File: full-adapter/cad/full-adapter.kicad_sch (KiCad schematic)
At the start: 0 parts

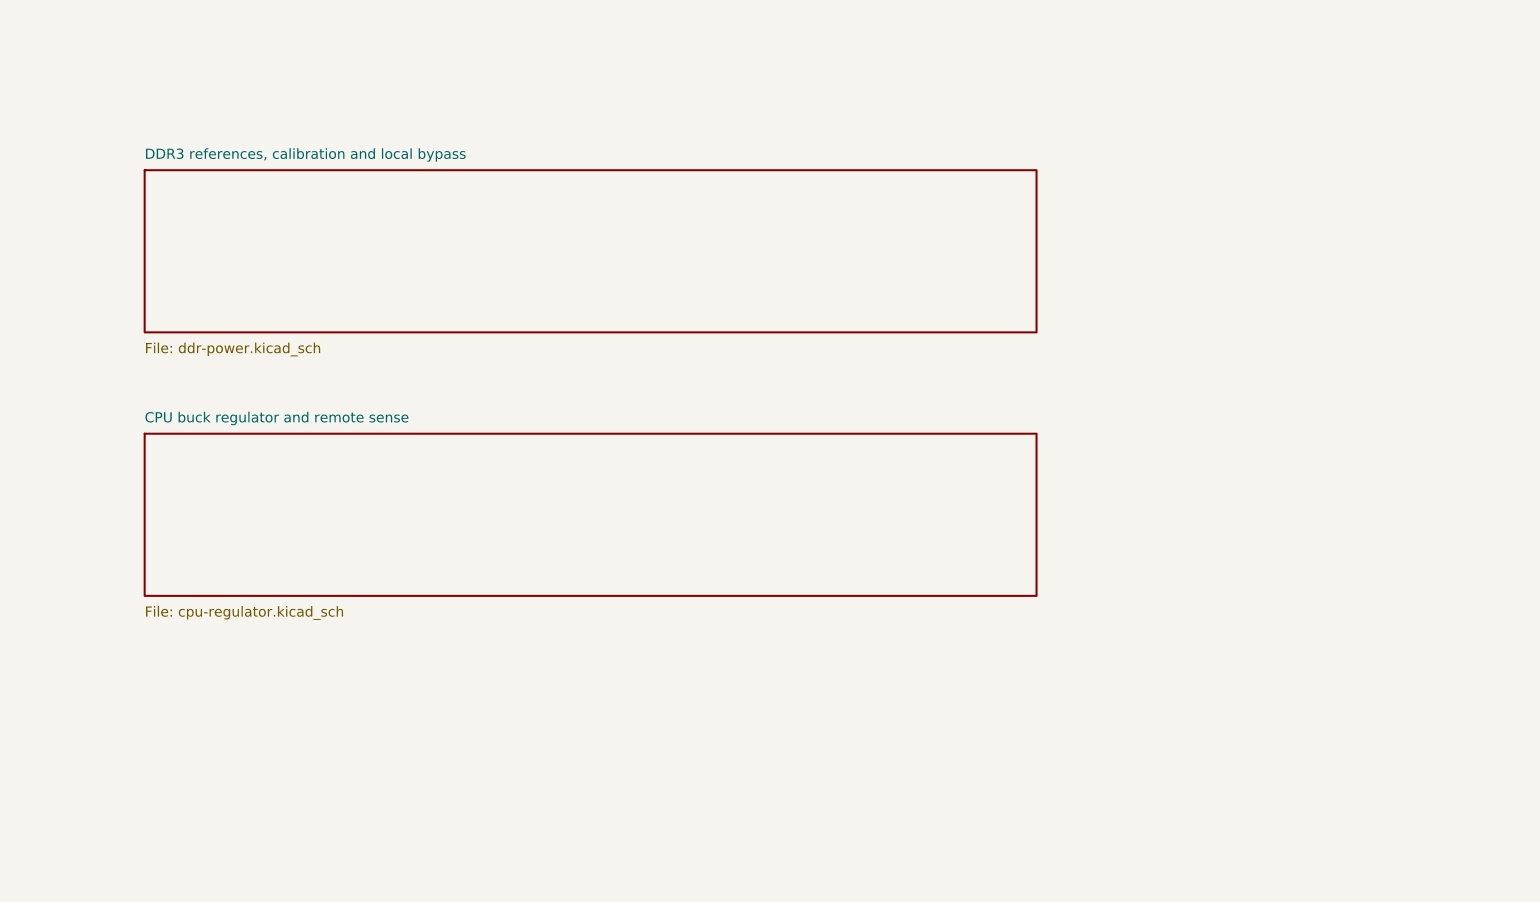
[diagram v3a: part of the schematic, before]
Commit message: Capture hardware-selected DDR3 buck and verify voltage corners
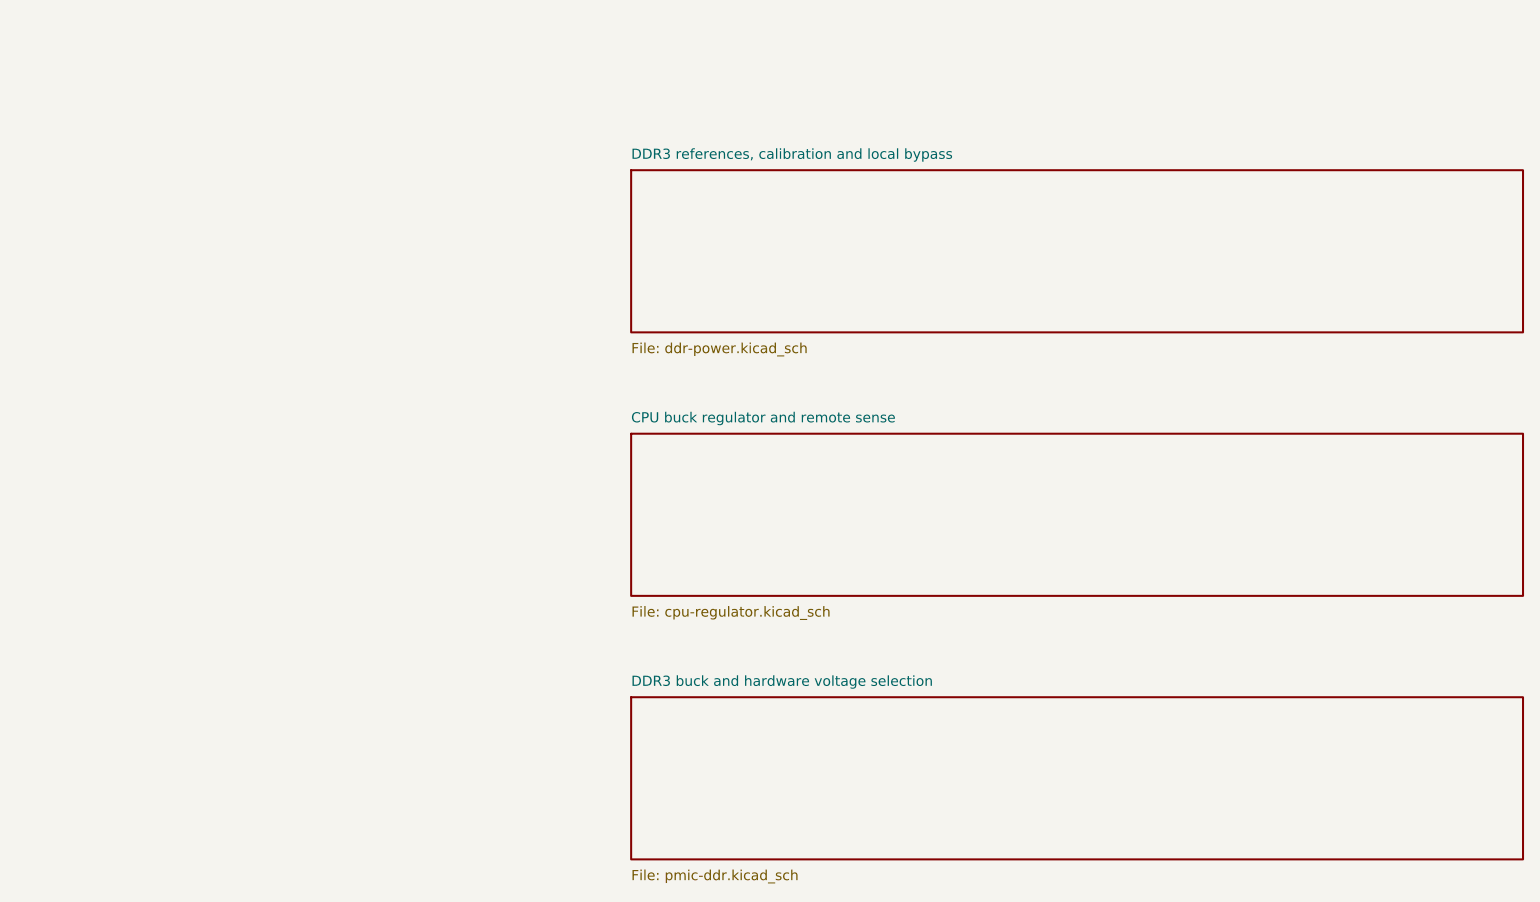
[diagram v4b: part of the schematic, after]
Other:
- added sheet DDR3 buck and hardware voltage selection (pmic-ddr.kicad_sch)
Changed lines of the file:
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@@
-(kicad_sch (version 20250114) (generator "full_adapter_schematic") (paper "A4")
+(kicad_sch (version 20250114) (generator "full_adapter_schematic") (paper "A3")
 (title_block (title "Integrated Linux USB3 modem / 2.5GbE development board") (rev "WORK IN PROGRESS") (company "Integrated modem development board"))
 (text "CURRENT DESIGN — IN PROGRESS" (at 20.32 20.32 0) (effects (font (size 2.54 2.54)) (justify left top)))
 (text "RK3568B2 + 1 GiB DDR3 + PCIe RTL8125BG-CG\nUSB3 M.2 modem; isolated PoE and USB-C auxiliary power\n\nDDR capture is present. Remaining subsystem capture and PCB routing\nare active work. This project is not a manufacturing release." (at 20.32 33.02 0) (effects (font (size 1.8 1.8)) (justify left top)))
 (sheet (at 25.4 88.9) (size 111.76 20.32) (fields_autoplaced yes) (stroke (width 0.254) (type default)) (fill (color 0 0 0 0)) (property "Sheetname" "1 GiB DDR3: command, data and clock termination" (at 25.4 87.63000000000001 0) (effects (font (size 1.27 1.27)) (justify left bottom))) (property "Sheetfile" "ddr-signals.kicad_sch" (at 25.4 110.49000000000001 0) (effects (font (size 1.27 1.27)) (justify left top))))
-(sheet (at 160.02 88.9) (size 111.76 20.32) (fields_autoplaced yes) (stroke (width 0.254) (type default)) (fill (color 0 0 0 0)) (property "Sheetname" "DDR3 references, calibration and local bypass" (at 160.02 87.63000000000001 0) (effects (font (size 1.27 1.27)) (justify left bottom))) (property "Sheetfile" "ddr-power.kicad_sch" (at 160.02 110.49000000000001 0) (effects (font (size 1.27 1.27)) (justify left top))))
+(sheet (at 220.98000000000002 88.9) (size 111.76 20.32) (fields_autoplaced yes) (stroke (width 0.254) (type default)) (fill (color 0 0 0 0)) (property "Sheetname" "DDR3 references, calibration and local bypass" (at 220.98000000000002 87.63000000000001 0) (effects (font (size 1.27 1.27)) (justify left bottom))) (property "Sheetfile" "ddr-power.kicad_sch" (at 220.98000000000002 110.49000000000001 0) (effects (font (size 1.27 1.27)) (justify left top))))
 (sheet (at 25.4 121.92000000000002) (size 111.76 20.32) (fields_autoplaced yes) (stroke (width 0.254) (type default)) (fill (color 0 0 0 0)) (property "Sheetname" "Processor core supplies and all ground balls" (at 25.4 120.65000000000002 0) (effects (font (size 1.27 1.27)) (justify left bottom))) (property "Sheetfile" "core-power.kicad_sch" (at 25.4 143.51000000000002 0) (effects (font (size 1.27 1.27)) (justify left top))))
-(sheet (at 160.02 121.92000000000002) (size 111.76 20.32) (fields_autoplaced yes) (stroke (width 0.254) (type default)) (fill (color 0 0 0 0)) (property "Sheetname" "CPU buck regulator and remote sense" (at 160.02 120.65000000000002 0) (effects (font (size 1.27 1.27)) (justify left bottom))) (property "Sheetfile" "cpu-regulator.kicad_sch" (at 160.02 143.51000000000002 0) (effects (font (size 1.27 1.27)) (justify left top))))
+(sheet (at 220.98000000000002 121.92000000000002) (size 111.76 20.32) (fields_autoplaced yes) (stroke (width 0.254) (type default)) (fill (color 0 0 0 0)) (property "Sheetname" "CPU buck regulator and remote sense" (at 220.98000000000002 120.65000000000002 0) (effects (font (size 1.27 1.27)) (justify left bottom))) (property "Sheetfile" "cpu-regulator.kicad_sch" (at 220.98000000000002 143.51000000000002 0) (effects (font (size 1.27 1.27)) (justify left top))))
 (sheet (at 25.4 154.94) (size 111.76 20.32) (fields_autoplaced yes) (stroke (width 0.254) (type default)) (fill (color 0 0 0 0)) (property "Sheetname" "PMIC LDO supplies and startup defaults" (at 25.4 153.67 0) (effects (font (size 1.27 1.27)) (justify left bottom))) (property "Sheetfile" "pmic-ldo.kicad_sch" (at 25.4 176.53 0) (effects (font (size 1.27 1.27)) (justify left top))))
+(sheet (at 220.98000000000002 154.94) (size 111.76 20.32) (fields_autoplaced yes) (stroke (width 0.254) (type default)) (fill (color 0 0 0 0)) (property "Sheetname" "DDR3 buck and hardware voltage selection" (at 220.98000000000002 153.67 0) (effects (font (size 1.27 1.27)) (justify left bottom))) (property "Sheetfile" "pmic-ddr.kicad_sch" (at 220.98000000000002 176.53 0) (effects (font (size 1.27 1.27)) (justify left top))))
 )

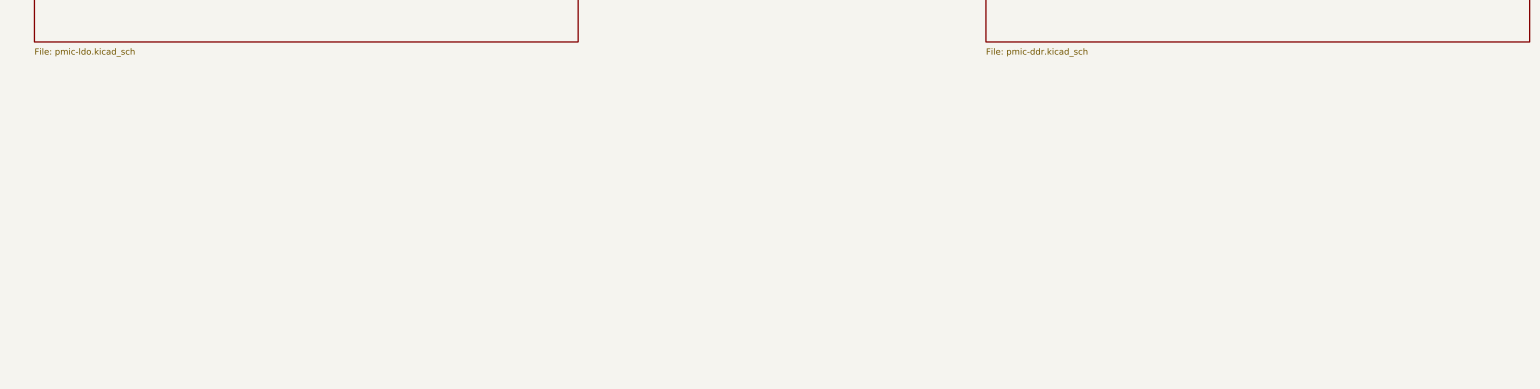
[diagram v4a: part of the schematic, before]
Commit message: Capture remaining PMIC bucks, supply switches and unused audio
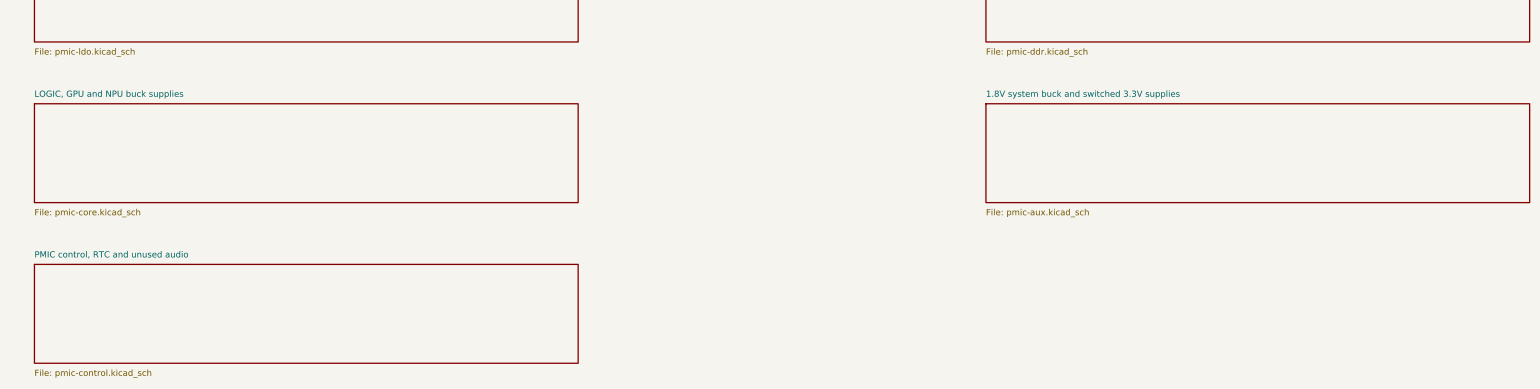
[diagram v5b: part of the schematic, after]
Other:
- added sheet 1.8V system buck and switched 3.3V supplies (pmic-aux.kicad_sch)
- added sheet LOGIC, GPU and NPU buck supplies (pmic-core.kicad_sch)
- added sheet PMIC control, RTC and unused audio (pmic-control.kicad_sch)
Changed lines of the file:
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@@
 (sheet (at 25.4 154.94) (size 111.76 20.32) (fields_autoplaced yes) (stroke (width 0.254) (type default)) (fill (color 0 0 0 0)) (property "Sheetname" "PMIC LDO supplies and startup defaults" (at 25.4 153.67 0) (effects (font (size 1.27 1.27)) (justify left bottom))) (property "Sheetfile" "pmic-ldo.kicad_sch" (at 25.4 176.53 0) (effects (font (size 1.27 1.27)) (justify left top))))
 (sheet (at 220.98000000000002 154.94) (size 111.76 20.32) (fields_autoplaced yes) (stroke (width 0.254) (type default)) (fill (color 0 0 0 0)) (property "Sheetname" "DDR3 buck and hardware voltage selection" (at 220.98000000000002 153.67 0) (effects (font (size 1.27 1.27)) (justify left bottom))) (property "Sheetfile" "pmic-ddr.kicad_sch" (at 220.98000000000002 176.53 0) (effects (font (size 1.27 1.27)) (justify left top))))
+(sheet (at 25.4 187.96) (size 111.76 20.32) (fields_autoplaced yes) (stroke (width 0.254) (type default)) (fill (color 0 0 0 0)) (property "Sheetname" "LOGIC, GPU and NPU buck supplies" (at 25.4 186.69 0) (effects (font (size 1.27 1.27)) (justify left bottom))) (property "Sheetfile" "pmic-core.kicad_sch" (at 25.4 209.55 0) (effects (font (size 1.27 1.27)) (justify left top))))
+(sheet (at 220.98000000000002 187.96) (size 111.76 20.32) (fields_autoplaced yes) (stroke (width 0.254) (type default)) (fill (color 0 0 0 0)) (property "Sheetname" "1.8V system buck and switched 3.3V supplies" (at 220.98000000000002 186.69 0) (effects (font (size 1.27 1.27)) (justify left bottom))) (property "Sheetfile" "pmic-aux.kicad_sch" (at 220.98000000000002 209.55 0) (effects (font (size 1.27 1.27)) (justify left top))))
+(sheet (at 25.4 220.98000000000002) (size 111.76 20.32) (fields_autoplaced yes) (stroke (width 0.254) (type default)) (fill (color 0 0 0 0)) (property "Sheetname" "PMIC control, RTC and unused audio" (at 25.4 219.71 0) (effects (font (size 1.27 1.27)) (justify left bottom))) (property "Sheetfile" "pmic-control.kicad_sch" (at 25.4 242.57000000000002 0) (effects (font (size 1.27 1.27)) (justify left top))))
 )
